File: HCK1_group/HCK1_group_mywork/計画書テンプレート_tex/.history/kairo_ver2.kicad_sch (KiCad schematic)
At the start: 4 parts, among them J1 Conn_01x08

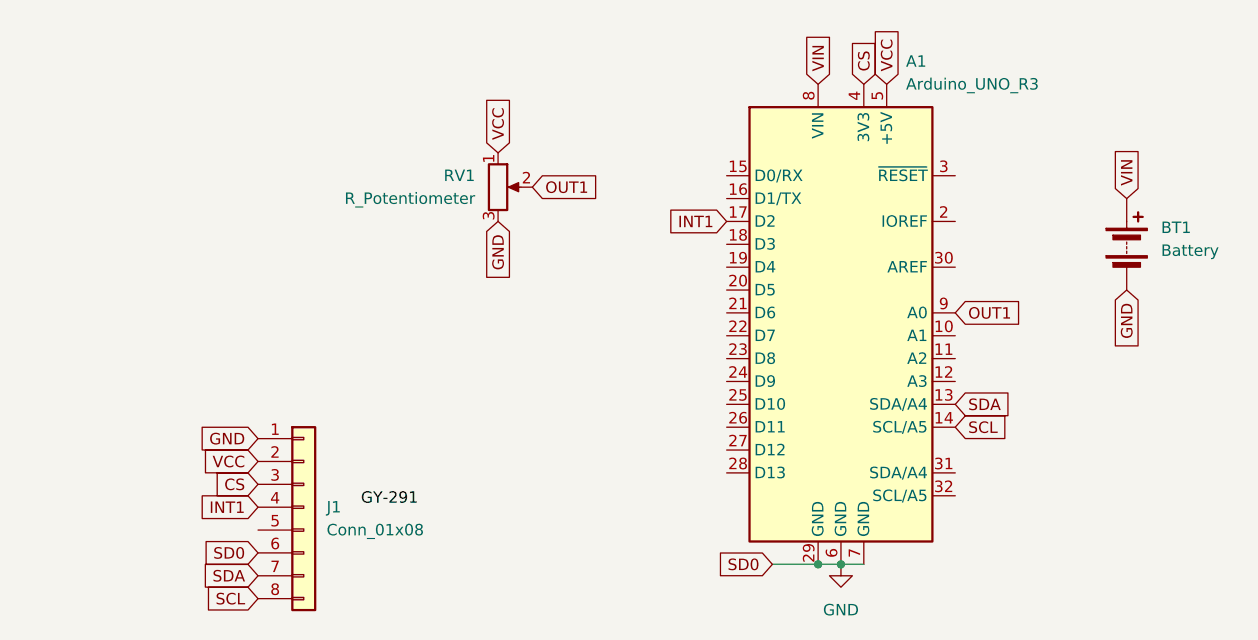
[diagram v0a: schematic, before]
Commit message: これまでの作業を反映: コード・計画書・回路図・作業ログ等を更新
- 指揮デバイス(shiki_device.ino): 音量用可変抵抗器をA5に変更、段階表示デバッグを改善
- 表示デバイス(Display.ino)、可変抵抗器検証(slider_test)を更新・追加
- 最終計画書・再計画書・設計関連ドキュメント、KiCad回路図を更新
- 第六/七回作業ログを整理、不要ファイル・旧資料を削除
- 設計用画像・図表を追加

注: ネストしたgitリポジトリ HCK1_group/yama は除外（別途submodule化が必要）

Co-Authored-By: Claude Opus 4.8 <noreply@anthropic.com>
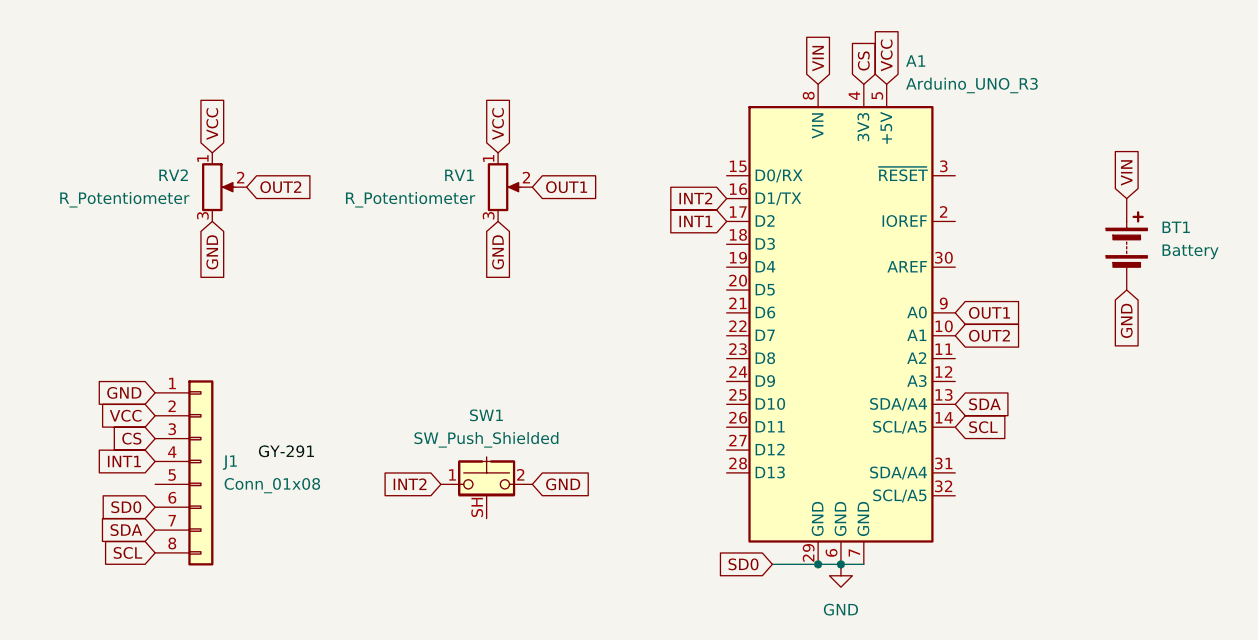
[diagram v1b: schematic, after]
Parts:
- added RV2: R_Potentiometer, symbol Device:R_Potentiometer
- added SW1: SW_Push_Shielded, symbol Switch:SW_Push_Shielded
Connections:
- net GND: now also RV2.3, SW1.2
- net VCC: now also RV2.1
- net OUT2: now reaches A1.10 (A1)
- net OUT2: now also RV2.2
- net INT2: now reaches A1.16 (D1/TX)
- net INT2: now also SW1.1
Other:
- moved on the sheet: J1
